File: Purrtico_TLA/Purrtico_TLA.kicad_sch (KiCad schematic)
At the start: 64 parts, among them J1 XLR3, J2 Conn_01x03, J3 Conn_01x02, J4 XLR3, J5 Conn_01x02, U1 OPA1679, U2 OPA1679

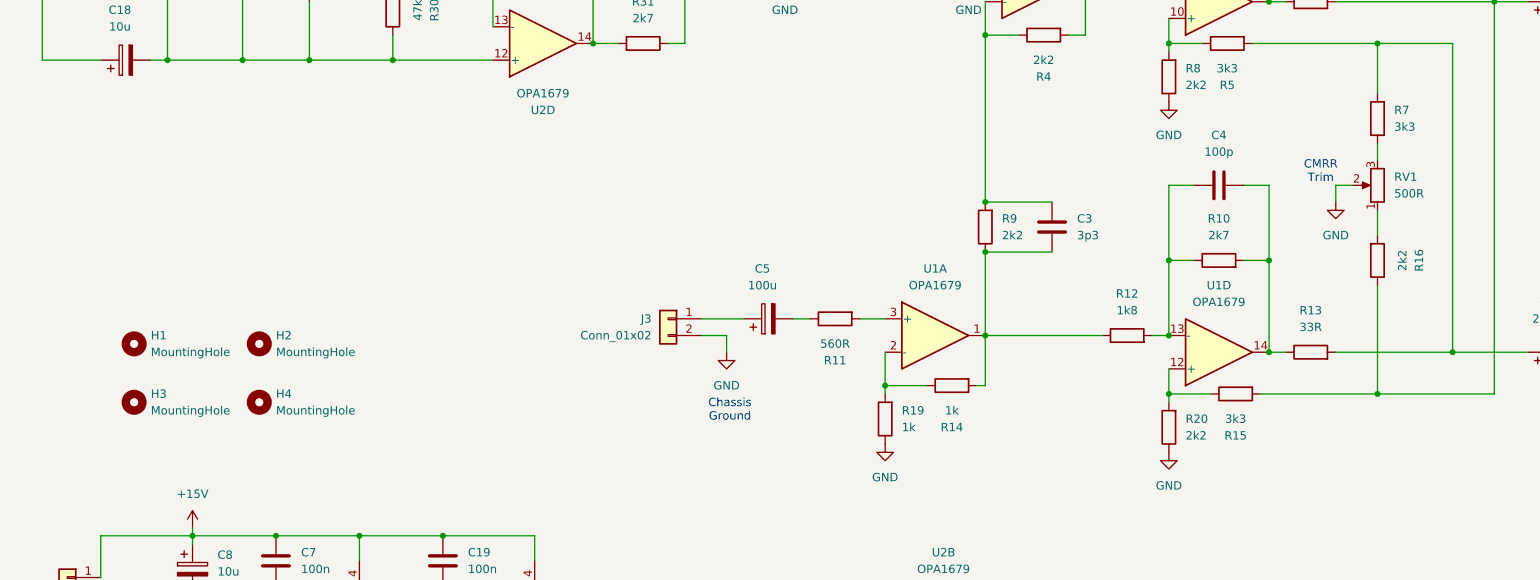
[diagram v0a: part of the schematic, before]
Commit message: 2k2 & mounting
made R7 & R16 equal value, added copper mounting holes
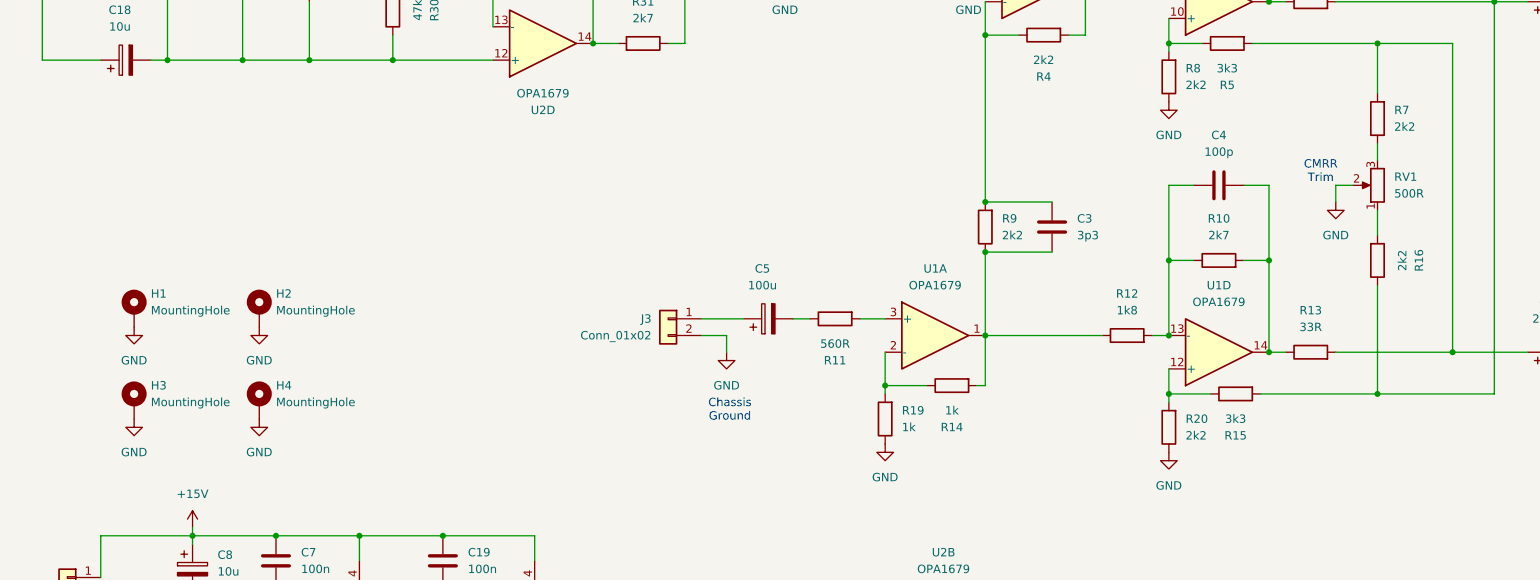
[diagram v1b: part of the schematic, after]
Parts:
- H1, H2, H3, H4: footprint MountingHole:MountingHole_3.2mm_M3_DIN965 -> MountingHole:MountingHole_3.2mm_M3_DIN965_Pad; symbol Mechanical:MountingHole -> Mechanical:MountingHole_Pad
- R7: value 3k3 -> 2k2
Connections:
- net GND: now also H1.1, H2.1, H3.1, H4.1

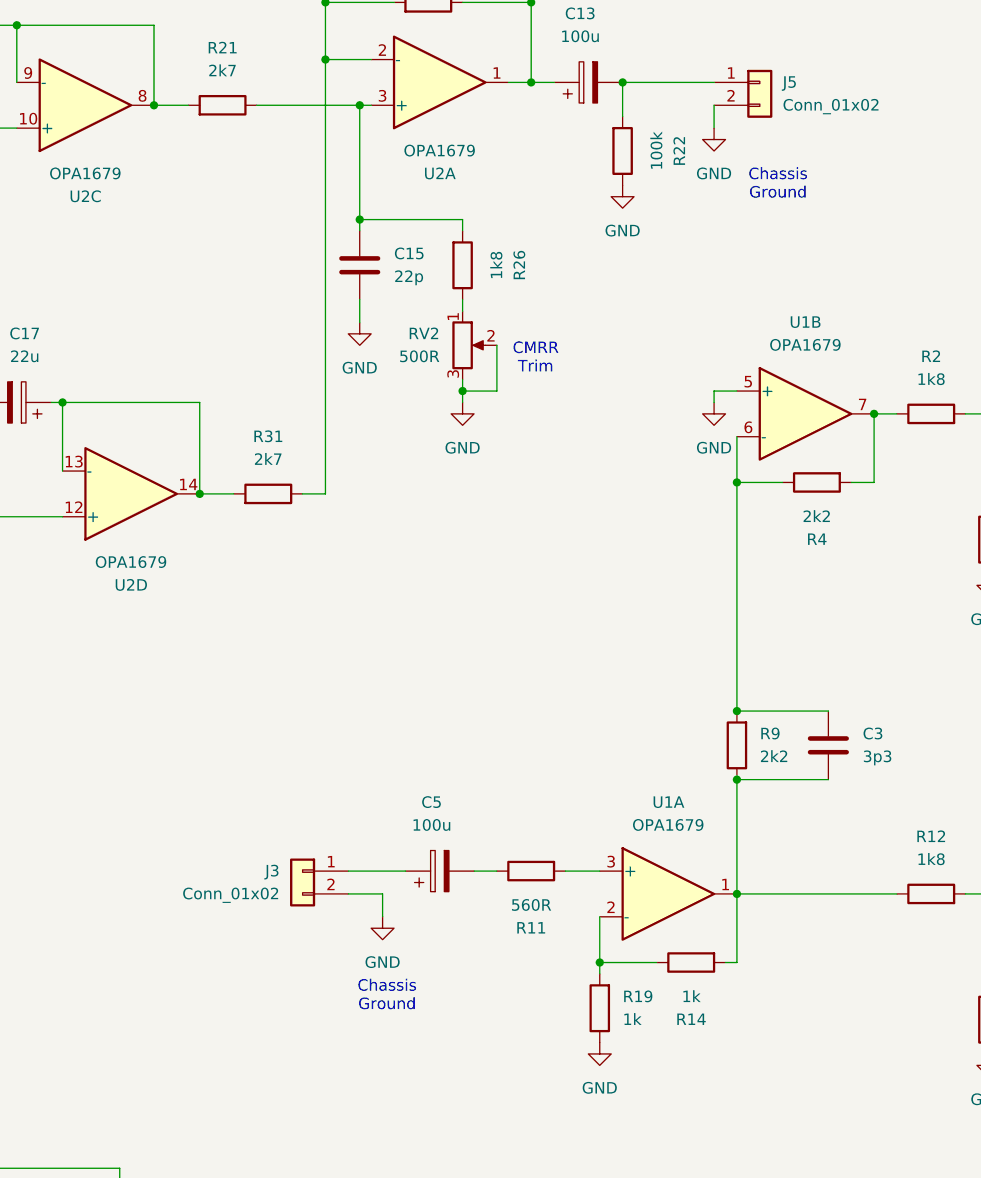
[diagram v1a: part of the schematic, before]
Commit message: input trim & teardrops
replaced 560R resistor with a 10k trim pot, added teardrops to THT- & IC-Pads
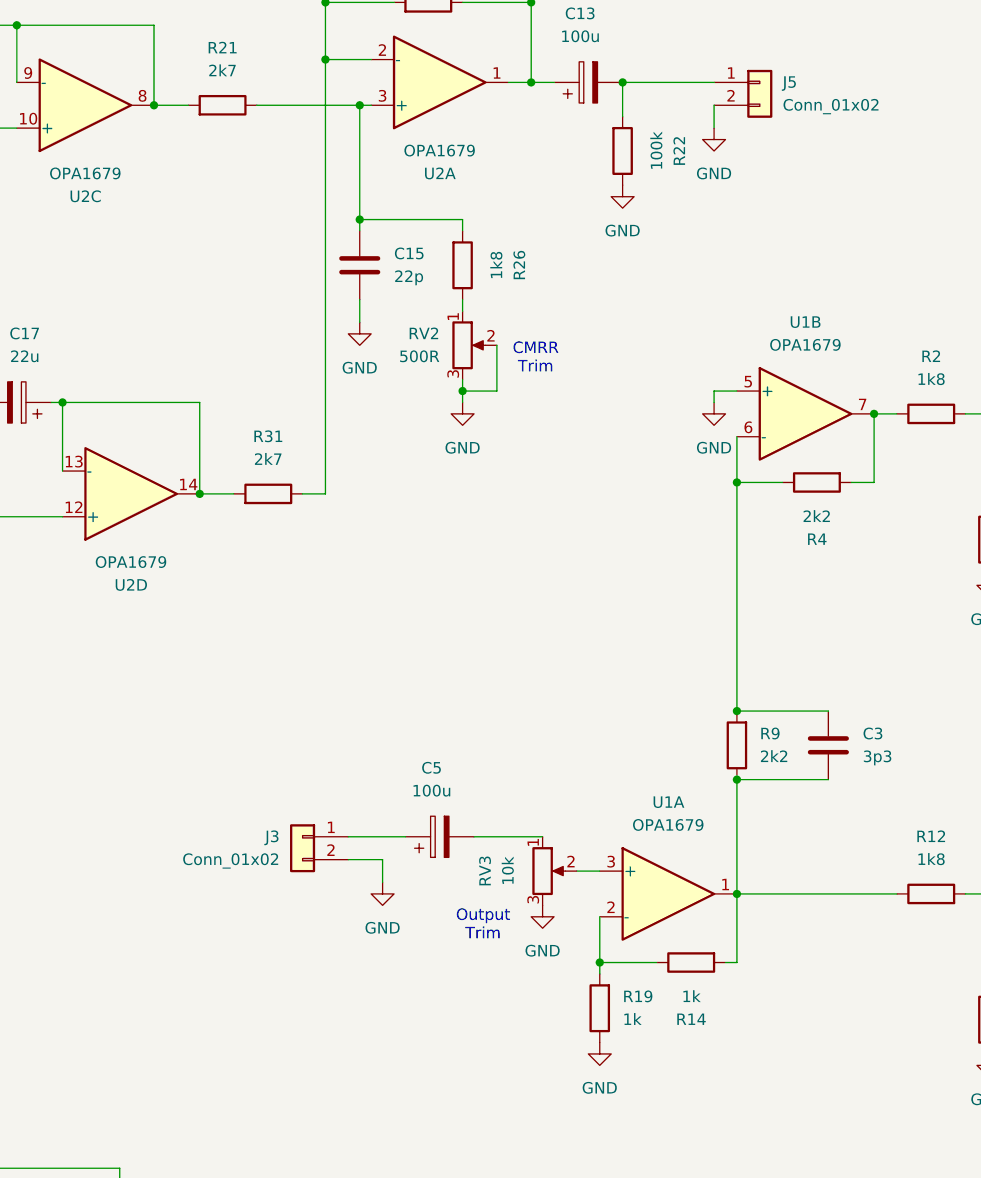
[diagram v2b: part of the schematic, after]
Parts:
- removed R11: 560R, Resistor_SMD:R_1206_3216Metric, symbol Device:R
- added RV3: 10k, Connector_PinHeader_2.54mm:PinHeader_1x03_P2.54mm_Vertical, symbol Device:R_Potentiometer
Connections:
- net GND: now also RV3.3
- net at U1.3 (+): now also RV3.2
- net at C5.2: now also RV3.1
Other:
- note added: "Output Trim"
- moved on the sheet: C5, J3
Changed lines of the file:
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@@
 	(wire
 		(pts
-			(xy 151.13 132.08) (xy 154.94 132.08)
-		)
-		(stroke
-			(width 0)
-			(type default)
-		)
-	)
-	(wire
-		(pts
 			(xy 49.53 176.53) (xy 49.53 179.07)
 		)
@@
 	(wire
 		(pts
-			(xy 127 134.62) (xy 130.81 134.62)
+			(xy 127 130.81) (xy 130.81 130.81)
 		)
 		(stroke
@@
 	(wire
 		(pts
-			(xy 127 132.08) (xy 133.35 132.08)
+			(xy 127 128.27) (xy 133.35 128.27)
 		)
 		(stroke
@@
 	(wire
 		(pts
+			(xy 152.4 132.08) (xy 154.94 132.08)
+		)
+		(stroke
+			(width 0)
+			(type default)
+		)
+	)
+	(wire
+		(pts
 			(xy 229.87 97.79) (xy 229.87 90.17)
 		)
@@
 	(wire
 		(pts
-			(xy 80.01 49.53) (xy 67.31 49.53)
+			(xy 140.97 128.27) (xy 148.59 128.27)
 		)
 		(stroke
@@
 	(wire
 		(pts
-			(xy 140.97 132.08) (xy 143.51 132.08)
+			(xy 80.01 49.53) (xy 67.31 49.53)
 		)
 		(stroke
@@
 	(wire
 		(pts
-			(xy 130.81 134.62) (xy 130.81 137.16)
+			(xy 130.81 130.81) (xy 130.81 133.35)
 		)
 		(stroke
@@
 		)
 	)
-	(text "Chassis\nGround"
-		(exclude_from_sim no)
-		(at 174.752 55.88 0)
-		(effects
-			(font
-				(size 1.27 1.27)
-			)
-		)
-	)
-	(text "Chassis\nGround"
-		(exclude_from_sim no)
-		(at 131.318 146.05 0)
-		(effects
-			(font
-				(size 1.27 1.27)
-			)
-		)
-	)
 	(text "CMRR\nTrim"
 		(exclude_from_sim no)
@@
 		)
 	)
+	(text "Output\nTrim"
+		(exclude_from_sim no)
+		(at 141.986 139.954 0)
+		(effects
+			(font
+				(size 1.27 1.27)
+			)
+			(justify bottom)
+		)
+	)
 	(symbol
 		(lib_id "Device:R")
@@
 	)
 	(symbol
+		(lib_name "GND_1")
+		(lib_id "power:GND")
+		(at 148.59 135.89 0)
+		(unit 1)
+		(exclude_from_sim no)
+		(in_bom yes)
+		(on_board yes)
+		(dnp no)
+		(fields_autoplaced yes)
+		(property "Reference" "#PWR027"
+			(at 148.59 142.24 0)
+			(effects
+				(font
+					(size 1.27 1.27)
+				)
+				(hide yes)
+			)
+		)
+		(property "Value" "GND"
+			(at 148.59 140.97 0)
+			(effects
+				(font
+					(size 1.27 1.27)
+				)
+			)
+		)
+		(property "Footprint" ""
+			(at 148.59 135.89 0)
+			(effects
+				(font
+					(size 1.27 1.27)
+				)
+				(hide yes)
+			)
+		)
+		(property "Datasheet" ""
+			(at 148.59 135.89 0)
+			(effects
+				(font
+					(size 1.27 1.27)
+				)
+				(hide yes)
+			)
+		)
+		(property "Description" "Power symbol creates a global label with name \"GND\" , ground"
+			(at 148.59 135.89 0)
+			(effects
+				(font
+					(size 1.27 1.27)
+				)
+				(hide yes)
+			)
+		)
+		(pin "1"
+		)
+		(instances
+			(project "Purrtico_TLA"
+				(path "/8744b698-520b-403d-9dc8-5ad840d7038f"
+					(reference "#PWR027")
+					(unit 1)
+				)
+			)
+		)
+	)
+	(symbol
 		(lib_id "Device:R")
 		(at 80.01 54.61 0)
@@
 	(symbol
 		(lib_id "Device:R")
-		(at 147.32 132.08 90)
-		(mirror x)
-		(unit 1)
-		(exclude_from_sim no)
-		(in_bom yes)
-		(on_board yes)
-		(dnp no)
-		(property "Reference" "R11"
-			(at 147.32 138.43 90)
-			(effects
-				(font
-					(size 1.27 1.27)
-				)
-			)
-		)
-		(property "Value" "560R"
-			(at 147.32 135.89 90)
-			(effects
-				(font
-					(size 1.27 1.27)
-				)
-			)
-		)
-		(property "Footprint" "Resistor_SMD:R_1206_3216Metric"
-			(at 147.32 130.302 90)
-			(effects
-				(font
-					(size 1.27 1.27)
-				)
-				(hide yes)
-			)
-		)
-		(property "Datasheet" "~"
-			(at 147.32 132.08 0)
-			(effects
-				(font
-					(size 1.27 1.27)
-				)
-				(hide yes)
-			)
-		)
-		(property "Description" ""
-			(at 147.32 132.08 0)
-			(effects
-				(font
-					(size 1.27 1.27)
-				)
-				(hide yes)
-			)
-		)
-		(pin "1"
-		)
-		(pin "2"
-		)
-		(instances
-			(project "Purrtico_TLA"
-				(path "/8744b698-520b-403d-9dc8-5ad840d7038f"
-					(reference "R11")
-					(unit 1)
-				)
-			)
-		)
-	)
-	(symbol
-		(lib_id "Device:R")
 		(at 229.87 123.19 0)
 		(mirror x)
@@
 	(symbol
 		(lib_id "Connector_Generic:Conn_01x02")
-		(at 121.92 132.08 0)
+		(at 121.92 128.27 0)
 		(mirror y)
 		(unit 1)
@@
 		(dnp no)
 		(property "Reference" "J3"
-			(at 119.38 132.0799 0)
+			(at 119.38 128.2699 0)
 			(effects
 				(font
@@
 		)
 		(property "Value" "Conn_01x02"
-			(at 119.38 134.6199 0)
+			(at 119.38 130.8099 0)
 			(effects
 				(font
@@
 		)
 		(property "Footprint" "Connector_PinHeader_2.54mm:PinHeader_1x02_P2.54mm_Vertical"
-			(at 121.92 132.08 0)
+			(at 121.92 128.27 0)
 			(effects
 				(font
@@
 		)
 		(property "Datasheet" "~"
-			(at 121.92 132.08 0)
+			(at 121.92 128.27 0)
 			(effects
 				(font
@@
 		)
 		(property "Description" "Generic connector, single row, 01x02, script generated (kicad-library-utils/schlib/autogen/connector/)"
-			(at 121.92 132.08 0)
+			(at 121.92 128.27 0)
 			(effects
 				(font
@@
 	)
 	(symbol
+		(lib_id "Device:R_Potentiometer")
+		(at 148.59 132.08 0)
+		(unit 1)
+		(exclude_from_sim no)
+		(in_bom yes)
+		(on_board yes)
+		(dnp no)
+		(property "Reference" "RV3"
+			(at 142.24 132.08 90)
+			(effects
+				(font
+					(size 1.27 1.27)
+				)
+			)
+		)
+		(property "Value" "10k"
+			(at 144.78 132.08 90)
+			(effects
+				(font
+					(size 1.27 1.27)
+				)
+			)
+		)
+		(property "Footprint" "Connector_PinHeader_2.54mm:PinHeader_1x03_P2.54mm_Vertical"
+			(at 148.59 132.08 0)
+			(effects
+				(font
+					(size 1.27 1.27)
+				)
+				(hide yes)
+			)
+		)
+		(property "Datasheet" "~"
+			(at 148.59 132.08 0)
+			(effects
+				(font
+					(size 1.27 1.27)
+				)
+				(hide yes)
+			)
+		)
+		(property "Description" ""
+			(at 148.59 132.08 0)
+			(effects
+				(font
+					(size 1.27 1.27)
+				)
+				(hide yes)
+			)
+		)
+		(pin "1"
+		)
+		(pin "2"
+		)
+		(pin "3"
+		)
+		(instances
+			(project "Purrtico_TLA"
+				(path "/8744b698-520b-403d-9dc8-5ad840d7038f"
+					(reference "RV3")
+					(unit 1)
+				)
+			)
+		)
+	)
+	(symbol
 		(lib_name "GND_1")
 		(lib_id "power:GND")
@@
 		(lib_name "GND_1")
 		(lib_id "power:GND")
-		(at 130.81 137.16 0)
+		(at 130.81 133.35 0)
 		(unit 1)
 		(exclude_from_sim no)
@@
 		(fields_autoplaced yes)
 		(property "Reference" "#PWR06"
-			(at 130.81 143.51 0)
+			(at 130.81 139.7 0)
 			(effects
 				(font
@@
 		)
 		(property "Value" "GND"
-			(at 130.81 142.24 0)
+			(at 130.81 138.43 0)
 			(effects
 				(font
@@
 		)
 		(property "Footprint" ""
-			(at 130.81 137.16 0)
+			(at 130.81 133.35 0)
 			(effects
 				(font
@@
 		)
 		(property "Datasheet" ""
-			(at 130.81 137.16 0)
+			(at 130.81 133.35 0)
 			(effects
 				(font
@@
 		)
 		(property "Description" "Power symbol creates a global label with name \"GND\" , ground"
-			(at 130.81 137.16 0)
+			(at 130.81 133.35 0)
 			(effects
 				(font
@@
 	(symbol
 		(lib_id "Device:C_Polarized")
-		(at 137.16 132.08 90)
+		(at 137.16 128.27 90)
 		(unit 1)
 		(exclude_from_sim no)
@@
 		(fields_autoplaced yes)
 		(property "Reference" "C5"
-			(at 136.271 124.46 90)
+			(at 136.271 120.65 90)
 			(effects
 				(font
@@
 		)
 		(property "Value" "100u"
-			(at 136.271 127 90)
+			(at 136.271 123.19 90)
 			(effects
 				(font
@@
 		)
 		(property "Footprint" "Capacitor_THT:CP_Radial_D6.3mm_P2.50mm"
-			(at 140.97 131.1148 0)
+			(at 140.97 127.3048 0)
 			(effects
 				(font
@@
 		)
 		(property "Datasheet" "~"
-			(at 137.16 132.08 0)
+			(at 137.16 128.27 0)
 			(effects
 				(font
@@
 		)
 		(property "Description" ""
-			(at 137.16 132.08 0)
+			(at 137.16 128.27 0)
 			(effects
 				(font

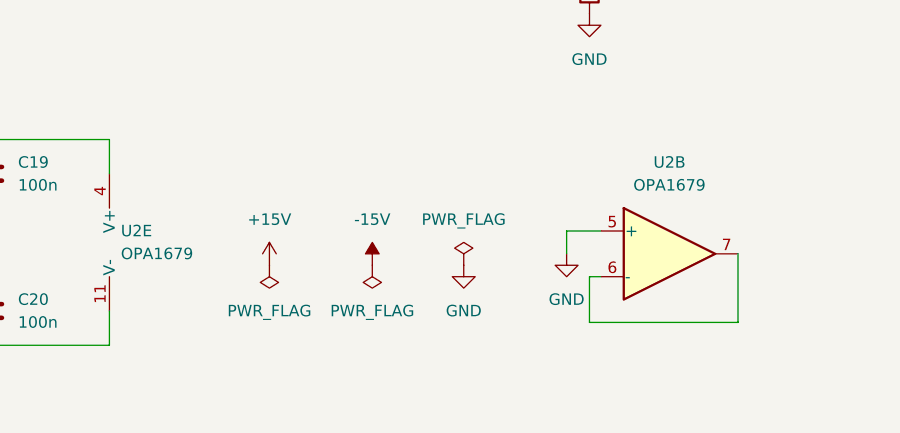
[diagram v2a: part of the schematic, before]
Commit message: added 0R resistors
added 0R resistors to make the unused opamp potentially usable
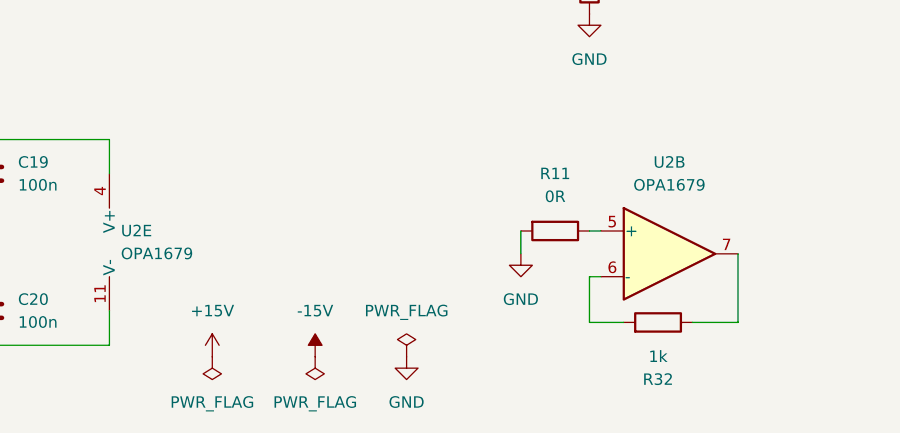
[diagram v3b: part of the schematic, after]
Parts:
- added R11: 0R, Resistor_SMD:R_1206_3216Metric, symbol Device:R
- added R32: 1k, Resistor_SMD:R_1206_3216Metric, symbol Device:R
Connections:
- net GND: now also R11.2; no longer U2.5 (+)
- net at U2.7: now also R32.1; no longer U2.6 (-)
- new net: R11.1, U2.5 (+)
- new net: R32.2, U2.6 (-)
